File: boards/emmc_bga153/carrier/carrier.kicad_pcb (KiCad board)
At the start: 4 copper layers, 12.5 x 14.6 mm, 2 parts, among them J1 DF40TC-30DP-0.4V(51), U1 EMMC_BGA153_INTERFACE

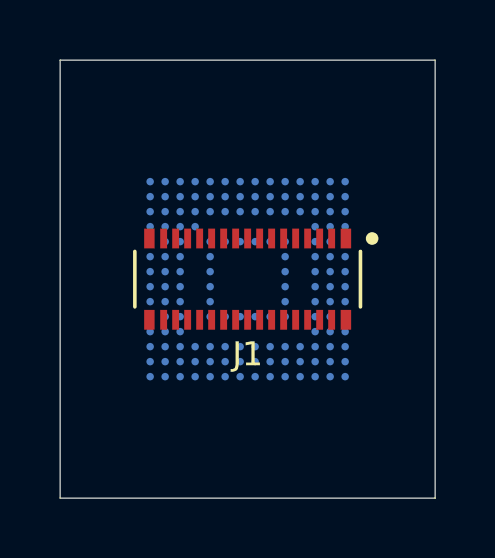
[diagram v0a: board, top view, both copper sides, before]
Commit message: Route eMMC BGA-153 carrier
27 of the 33 netted balls escape: row A straight out of the field, the inner
ring into the vacant 4x4 block, rows C and M through the vacant moat, and the
outer ring to the pours.  0 DRC errors, and check_generic's via keep-outs and
J1 net map still hold.

/DAT3-/DAT7 (balls B2-B6) and the GND ball N2 are BLOCKED and left unrouted.
Rows A-C and M-P are fully populated, so those balls sit behind an unbroken
wall of lands, and at 0.5 mm pitch nothing legal passes between two adjacent
0.25 mm lands: the gate offers 0.250 mm from its centreline to each land
centre and the board minimum trace at the board minimum clearance needs
0.125 + 0.045 + 0.090 = 0.260 mm.  The interstitial saddle (0.354 mm) fits a
trace and would fit JLC's own 0.25/0.15 BGA via on copper (0.350 mm), but the
project's global 0.20 mm hole clearance -- quoted from JLC's *inner layer*
via-hole-to-copper row -- demands 0.400 mm, where their BGA table's row D
gives drill-to-BGA-pad as 0 mm.  Unblocking those six balls is a rules
decision (scoped .dru exception, via-in-pad, or a smaller land), so it is
left to the user; see the task report.

tools/dogbones.py generalizes add_courk_dogbones: the via, its clearances and
the candidate lattice are all parameters, the hole-clearance floor is modelled
(it is the binding one at 0.5 mm pitch, and the 0.8 mm original never needed
it), and it reports what it cannot place with the failing distance instead of
asserting.  tools/route_emmc_carrier.py holds this board's escape plan as a
declarative table, re-checks every via and stub through dogbones, and is
idempotent.

carrier.kicad_pro's netclasses were KiCad defaults (0.2 mm clearance,
0.6/0.3 vias), which cannot route this pitch at all -- a via on a vacant ball
site has 0.150 mm of clearance to its neighbour.  They now mirror the shipped
VFBGA67 carrier: 0.10 mm clearance, 0.45/0.20 vias, Signal/Power patterns.

Co-Authored-By: Claude Fable 5 <noreply@anthropic.com>
Claude-Session: https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
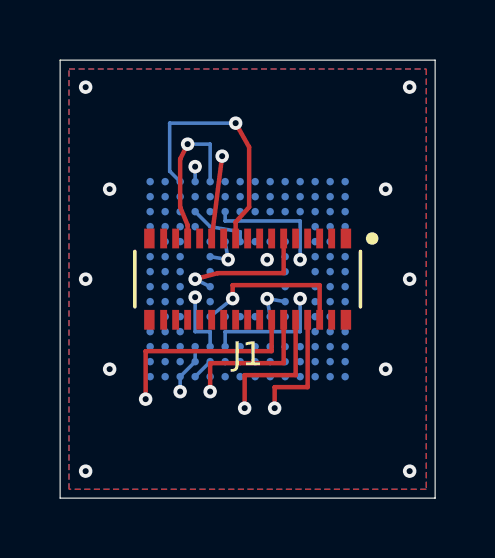
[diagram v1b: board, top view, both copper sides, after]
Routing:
- net /CLK: track 0.00 -> 24.2 mm, vias 0 -> 2
- net VCCQ: track 0.00 -> 23.9 mm, vias 0 -> 3
- net VCC: track 0.00 -> 12.7 mm, vias 0 -> 3
- net /CMD: track 0.00 -> 11.1 mm, vias 0 -> 2
- net /DAT0: track 0.00 -> 8.43 mm, vias 0 -> 1
- net /RST_n: track 0.00 -> 5.47 mm, vias 0 -> 1
- net /DAT2: track 0.00 -> 5.25 mm, vias 0 -> 1
- net /DS: track 0.00 -> 4.69 mm, vias 0 -> 1
- net /DAT1: track 0.00 -> 4.23 mm, vias 0 -> 2
- net GND: track 0.00 -> 2.76 mm, vias 0 -> 11
- added copper zone on B.Cu, net GND
- added copper zone on F.Cu, net GND
- added copper zone on In2.Cu, net GND
